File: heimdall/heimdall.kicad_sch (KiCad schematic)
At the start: 28 parts, among them J1 Conn_01x04, J2 USB_C_Receptacle_USB2.0, J3 Conn_01x05, U1 STM32F072CBT6, U2 PRTR5V0U2X, U4 TXB0101

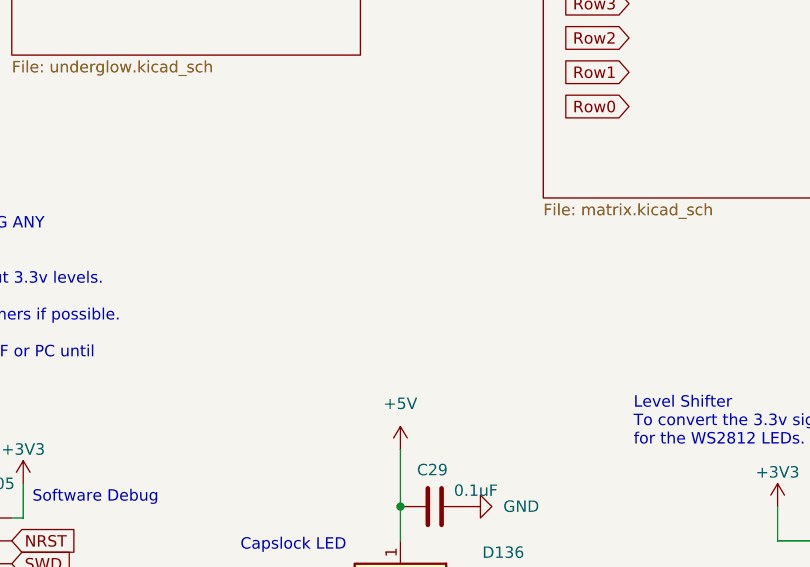
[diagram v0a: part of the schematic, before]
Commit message: Finished routing the left side 100%
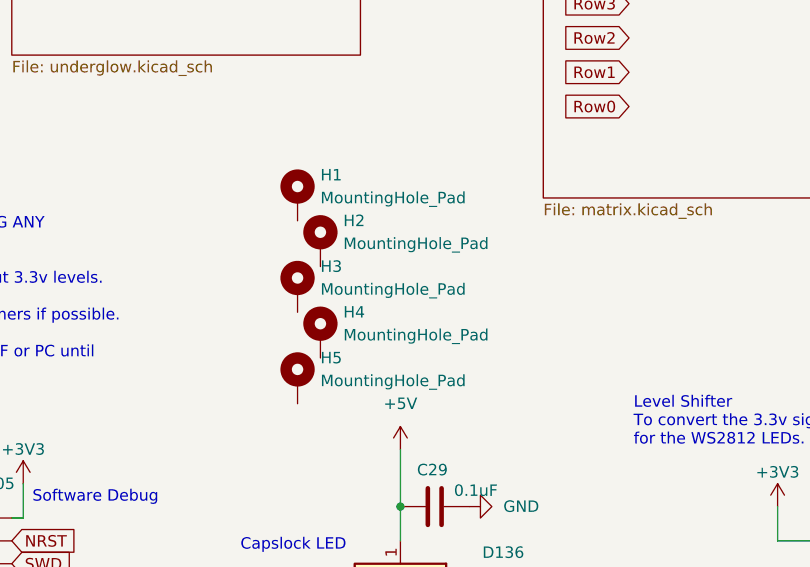
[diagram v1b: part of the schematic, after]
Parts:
- added H1, H2, H3, H4, H5: MountingHole_Pad, MountingHole:MountingHole_3.2mm_M3, symbol Mechanical:MountingHole_Pad
